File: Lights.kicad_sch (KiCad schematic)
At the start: 32 parts, among them J3 Conn_01x12, J4 Conn_02x06_Odd_Even, Q1 2N7002, Q2 2N7002, Q3 2N7002, Q4 2N7002, Q5 2N7002, Q6 2N7002, U2 EL3H7, U3 EL3H7, U4 EL3H7, U5 EL3H7, U6 EL3H7, U7 EL3H7

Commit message: prelim board layout
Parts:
- removed J3: Conn_01x12, symbol Connector_Generic:Conn_01x12
- removed J4: Conn_02x06_Odd_Even, symbol Connector_Generic:Conn_02x06_Odd_Even
- renumbered L_XTRA1_EXT to L_XTRA1_EXT1, R_XTRA1_EXT to R_XTRA1_EXT1
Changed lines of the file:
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@@
 	)
 	(symbol
-		(lib_id "Connector_Generic:Conn_02x06_Odd_Even")
-		(at 212.09 60.96 0)
-		(unit 1)
-		(exclude_from_sim no)
-		(in_bom yes)
-		(on_board yes)
-		(dnp no)
-		(fields_autoplaced yes)
-		(property "Reference" "J4"
-			(at 213.36 49.53 0)
-			(effects
-				(font
-					(size 1.27 1.27)
-				)
-			)
-		)
-		(property "Value" "Conn_02x06_Odd_Even"
-			(at 213.36 52.07 0)
-			(effects
-				(font
-					(size 1.27 1.27)
-				)
-			)
-		)
-		(property "Footprint" ""
-			(at 212.09 60.96 0)
-			(effects
-				(font
-					(size 1.27 1.27)
-				)
-				(hide yes)
-			)
-		)
-		(property "Datasheet" "~"
-			(at 212.09 60.96 0)
-			(effects
-				(font
-					(size 1.27 1.27)
-				)
-				(hide yes)
-			)
-		)
-		(property "Description" "Generic connector, double row, 02x06, odd/even pin numbering scheme (row 1 odd numbers, row 2 even numbers), script generated (kicad-library-utils/schlib/autogen/connector/)"
-			(at 212.09 60.96 0)
-			(effects
-				(font
-					(size 1.27 1.27)
-				)
-				(hide yes)
-			)
-		)
-		(pin "5"
-		)
-		(pin "1"
-		)
-		(pin "10"
-		)
-		(pin "11"
-		)
-		(pin "9"
-		)
-		(pin "12"
-		)
-		(pin "6"
-		)
-		(pin "8"
-		)
-		(pin "2"
-		)
-		(pin "7"
-		)
-		(pin "4"
-		)
-		(pin "3"
-		)
-		(instances
-			(project ""
-				(path "/229b82f0-5048-47d6-8bc8-0bcee42eb4bc/ceb5a95e-a274-4dea-8a59-96d1af6e854d"
-					(reference "J4")
-					(unit 1)
-				)
-			)
-		)
-	)
-	(symbol
 		(lib_id "Transistor_FET:2N7002")
 		(at 90.17 135.89 0)
@@
 		(on_board yes)
 		(dnp no)
-		(property "Reference" "R_XTRA1_EXT"
+		(property "Reference" "R_XTRA1_EXT1"
 			(at 255.778 126.746 0)
 			(effects
@@
 			(project "Controls-LightingPCB"
 				(path "/229b82f0-5048-47d6-8bc8-0bcee42eb4bc/ceb5a95e-a274-4dea-8a59-96d1af6e854d"
-					(reference "R_XTRA1_EXT")
-					(unit 1)
-				)
-			)
-		)
-	)
-	(symbol
-		(lib_id "Connector_Generic:Conn_01x12")
-		(at 173.99 68.58 0)
-		(unit 1)
-		(exclude_from_sim no)
-		(in_bom yes)
-		(on_board yes)
-		(dnp no)
-		(fields_autoplaced yes)
-		(property "Reference" "J3"
-			(at 176.53 68.5799 0)
-			(effects
-				(font
-					(size 1.27 1.27)
-				)
-				(justify left)
-			)
-		)
-		(property "Value" "Conn_01x12"
-			(at 176.53 71.1199 0)
-			(effects
-				(font
-					(size 1.27 1.27)
-				)
-				(justify left)
-			)
-		)
-		(property "Footprint" ""
-			(at 173.99 68.58 0)
-			(effects
-				(font
-					(size 1.27 1.27)
-				)
-				(hide yes)
-			)
-		)
-		(property "Datasheet" "~"
-			(at 173.99 68.58 0)
-			(effects
-				(font
-					(size 1.27 1.27)
-				)
-				(hide yes)
-			)
-		)
-		(property "Description" "Generic connector, single row, 01x12, script generated (kicad-library-utils/schlib/autogen/connector/)"
-			(at 173.99 68.58 0)
-			(effects
-				(font
-					(size 1.27 1.27)
-				)
-				(hide yes)
-			)
-		)
-		(pin "7"
-		)
-		(pin "8"
-		)
-		(pin "10"
-		)
-		(pin "12"
-		)
-		(pin "9"
-		)
-		(pin "2"
-		)
-		(pin "5"
-		)
-		(pin "11"
-		)
-		(pin "6"
-		)
-		(pin "1"
-		)
-		(pin "3"
-		)
-		(pin "4"
-		)
-		(instances
-			(project ""
-				(path "/229b82f0-5048-47d6-8bc8-0bcee42eb4bc/ceb5a95e-a274-4dea-8a59-96d1af6e854d"
-					(reference "J3")
+					(reference "R_XTRA1_EXT1")
 					(unit 1)
 				)
@@
 		(on_board yes)
 		(dnp no)
-		(property "Reference" "L_XTRA1_EXT"
+		(property "Reference" "L_XTRA1_EXT1"
 			(at 257.048 94.996 0)
 			(effects
@@
 			(project "Controls-LightingPCB"
 				(path "/229b82f0-5048-47d6-8bc8-0bcee42eb4bc/ceb5a95e-a274-4dea-8a59-96d1af6e854d"
-					(reference "L_XTRA1_EXT")
+					(reference "L_XTRA1_EXT1")
 					(unit 1)
 				)

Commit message: updated prelim
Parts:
- removed Q1, Q2, Q3, Q4, Q5, Q6: 2N7002, Package_TO_SOT_SMD:SOT-23, symbol Transistor_FET:2N7002
- added Q1, Q2, Q3, Q4, Q5, Q6: IRLML0030, Package_TO_SOT_SMD:SOT-23, symbol Transistor_FET:IRLML0030
- R1, R11, R2, R5, R7, R9: value 698 -> 1k
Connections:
- net GNDPWR: now also Q1.2 (S), Q2.2 (S), Q3.2 (S), Q4.2 (S), Q5.2 (S), Q6.2 (S)
- net at R10.1, U6.3: now also Q3.1 (G)
- net at L_XTRA2_EXT1.2 (Pin_2): now also Q3.3 (D)
- net at R3.2, U2.3: now also Q1.1 (G)
- net at R_XTRA2_EXT2.2 (Pin_2): now also Q4.3 (D)
- net at R4.1, U3.3: now also Q2.1 (G)
- net at L_BLINK_EXT1.2 (Pin_2): now also Q2.3 (D)
- net at R_BLINK_EXT1.2 (Pin_2): now also Q1.3 (D)
- net at R8.1, U5.3: now also Q6.1 (G)
- net at R12.1, U7.3: now also Q4.1 (G)
- net at R_XTRA1_EXT1.2 (Pin_2): now also Q6.3 (D)
- net at R6.1, U4.3: now also Q5.1 (G)
- net at L_XTRA1_EXT1.2 (Pin_2): now also Q5.3 (D)

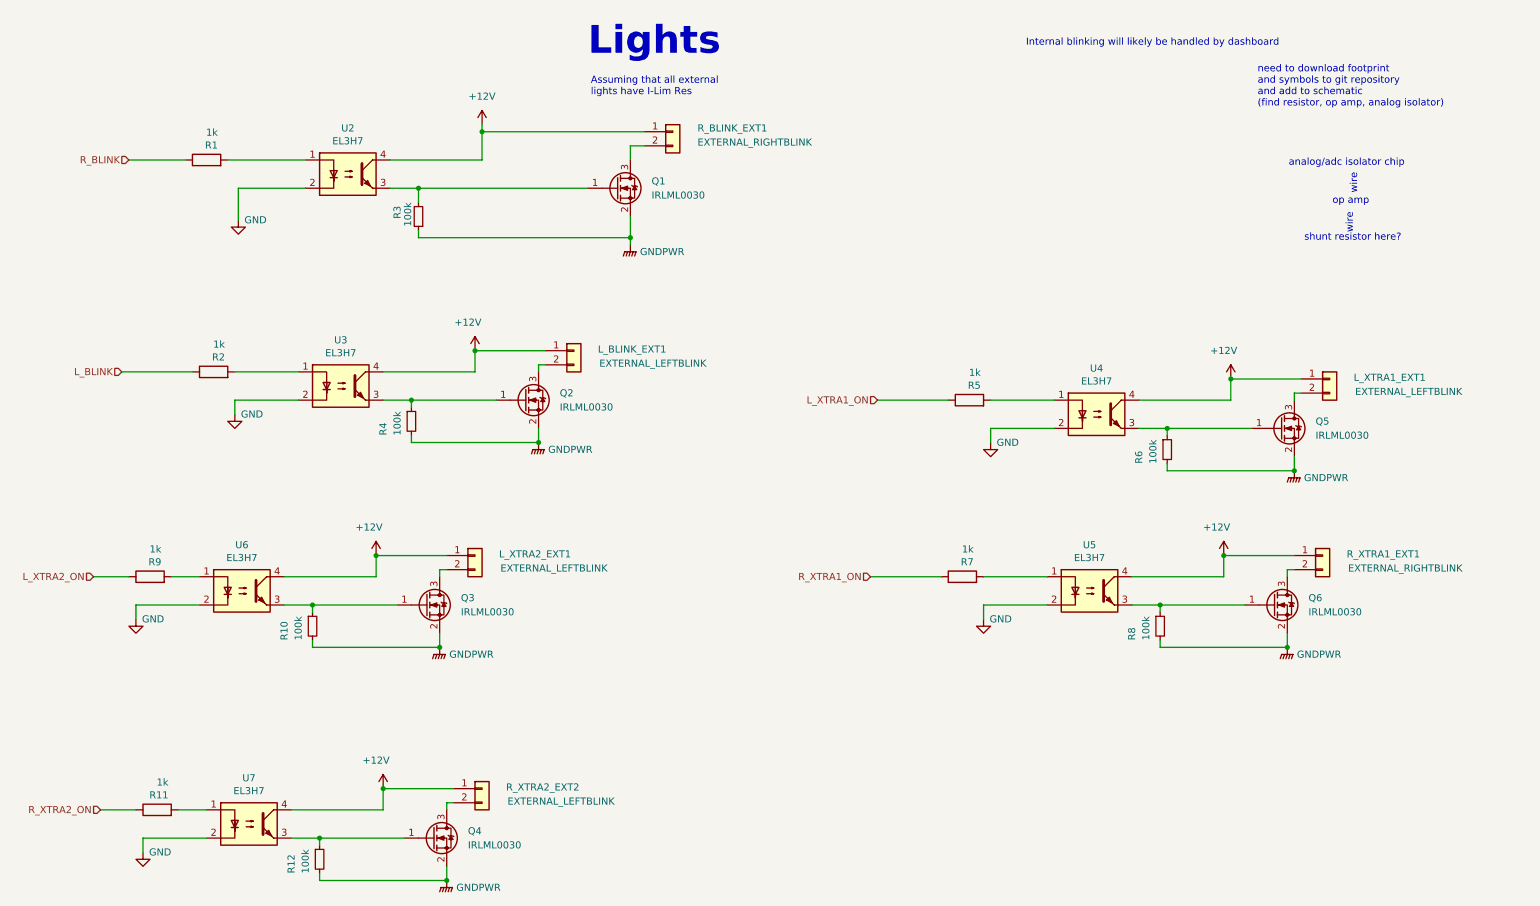
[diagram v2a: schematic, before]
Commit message: layout before connecting traces
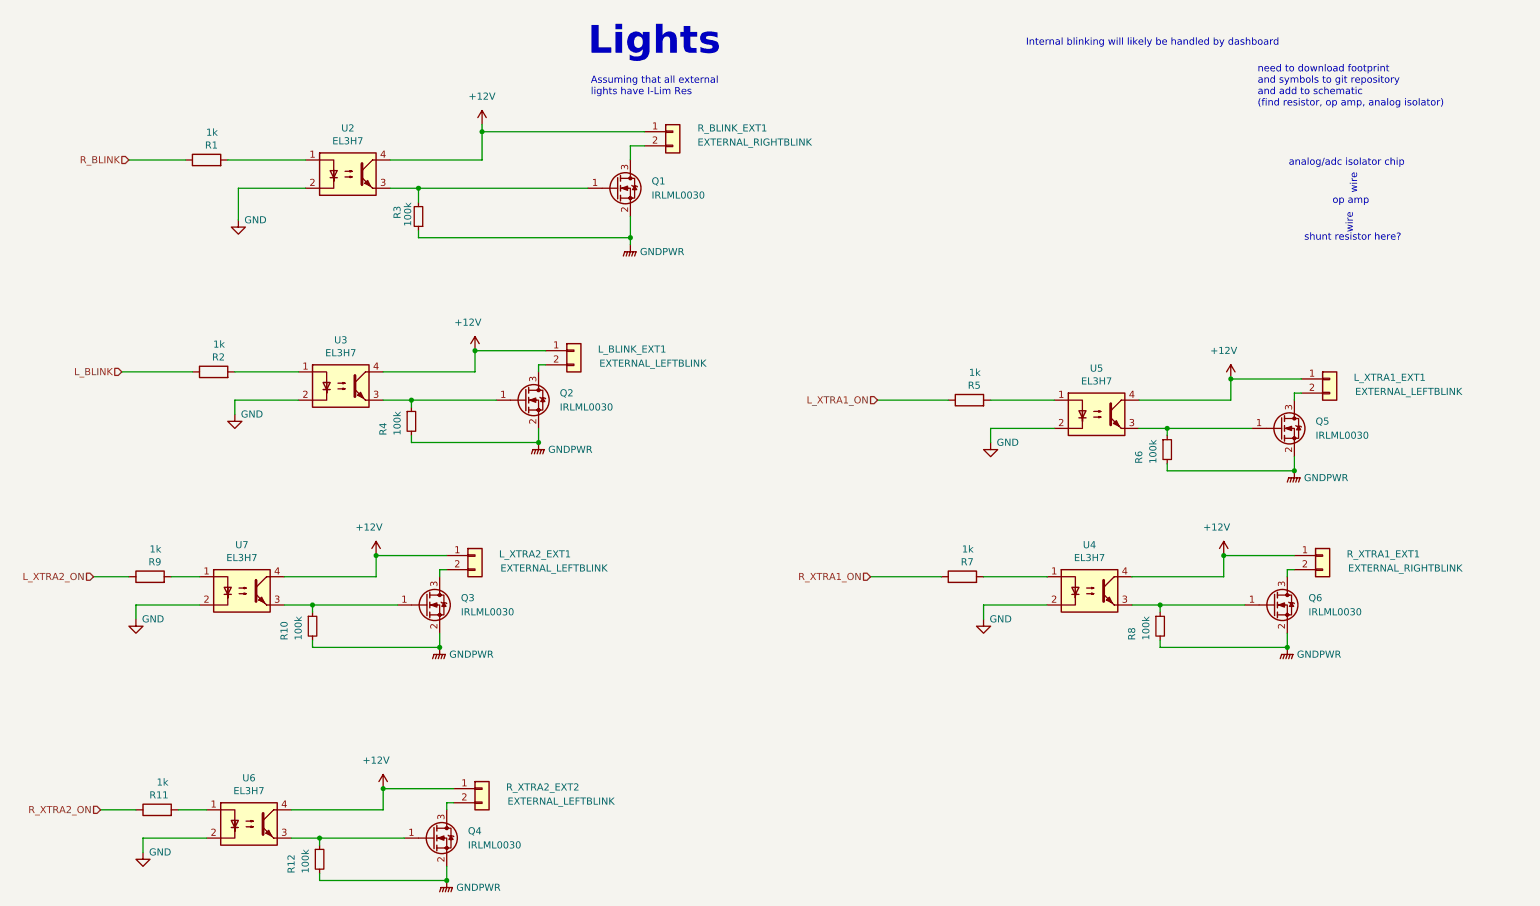
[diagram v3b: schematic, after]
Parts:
- renumbered U5 to U4, U4 to U5, U7 to U6, U6 to U7
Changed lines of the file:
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@@
 		(on_board yes)
 		(dnp no)
-		(property "Reference" "U7"
+		(property "Reference" "U6"
 			(at 58.42 167.005 0)
 			(effects
@@
 			(project "Controls-LightingPCB"
 				(path "/229b82f0-5048-47d6-8bc8-0bcee42eb4bc/ceb5a95e-a274-4dea-8a59-96d1af6e854d"
-					(reference "U7")
+					(reference "U6")
 					(unit 1)
 				)
@@
 		(on_board yes)
 		(dnp no)
-		(property "Reference" "U6"
+		(property "Reference" "U7"
 			(at 57.15 125.095 0)
 			(effects
@@
 			(project "Controls-LightingPCB"
 				(path "/229b82f0-5048-47d6-8bc8-0bcee42eb4bc/ceb5a95e-a274-4dea-8a59-96d1af6e854d"
-					(reference "U6")
+					(reference "U7")
 					(unit 1)
 				)
@@
 		(on_board yes)
 		(dnp no)
-		(property "Reference" "U5"
+		(property "Reference" "U4"
 			(at 209.55 125.095 0)
 			(effects
@@
 			(project "Controls-LightingPCB"
 				(path "/229b82f0-5048-47d6-8bc8-0bcee42eb4bc/ceb5a95e-a274-4dea-8a59-96d1af6e854d"
-					(reference "U5")
+					(reference "U4")
 					(unit 1)
 				)
@@
 		(on_board yes)
 		(dnp no)
-		(property "Reference" "U4"
+		(property "Reference" "U5"
 			(at 210.82 93.345 0)
 			(effects
@@
 			(project "Controls-LightingPCB"
 				(path "/229b82f0-5048-47d6-8bc8-0bcee42eb4bc/ceb5a95e-a274-4dea-8a59-96d1af6e854d"
-					(reference "U4")
-					(unit 1)
-				)
+					(reference "U5")
+					(unit 1)
+				)

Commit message: board rewire (ongoing)
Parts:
- R_XTRA2_EXT2: value EXTERNAL_LEFTBLINK -> EXTERNAL_RIGHTBLINK
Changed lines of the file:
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@@
 			)
 		)
-		(property "Value" "EXTERNAL_LEFTBLINK"
+		(property "Value" "EXTERNAL_RIGHTBLINK"
 			(at 104.902 171.196 0)
 			(effects
